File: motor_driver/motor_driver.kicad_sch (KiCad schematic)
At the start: 65 parts, among them J1 Conn_01x01_Socket, J2 Conn_01x01_Socket, J3 Conn_01x01_Socket, J4 Conn_01x03_Pin, J5 Conn_01x06_Pin, Q1 STB19NF20_T-220, Q2 STB19NF20_T-220, Q3 STB19NF20_T-220, Q4 STB19NF20_T-220, Q5 STB19NF20_T-220, Q6 STB19NF20_T-220, U1 INA241A2xD, U3 IR2110, U4 INA241A2xD, U6 IR2110, U7 INA241A2xD, U9 IR2110

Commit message: Change to isolation amp
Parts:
- removed D2: 1N4007, Diode_THT:D_DO-41_SOD81_P10.16mm_Horizontal, symbol Diode:1N4007
- removed J1, J2, J3: Conn_01x01_Socket, symbol Connector:Conn_01x01_Socket
- removed J4: Conn_01x03_Pin, Connector_PinHeader_2.54mm:PinHeader_1x03_P2.54mm_Vertical, symbol Connector:Conn_01x03_Pin
- removed R12, R19: R_Shunt, Custom_footprints:BVT-I-R003, symbol Device:R_Shunt
- removed U1, U4, U7: INA241A2xD, Package_SO:SOIC-8_3.9x4.9mm_P1.27mm, symbol Amplifier_Current:INA241A2xD
- removed U5, U8: ~, Custom_footprints:MCT6, symbol Custom_schematics:MCT6
- removed U6, U9: IR2110, Package_DIP:DIP-14_W7.62mm, symbol Driver_FET:IR2110
- added C22, C35: 10nF, symbol Device:C
- added C23, C26, C27, C29, C31, C33, C36, C39: 100nF, symbol Device:C
- added C24, C28, C32, C34, C37: 22uF, symbol Device:C
- added C25, C30, C38: 330pF, symbol Device:C
- added D2, D4, D6: BZX384xxxx, Diode_SMD:D_SOD-323, symbol Diode:BZX384xxxx
- added D5: 1N4007, Diode_THT:D_DO-41_SOD81_P10.16mm_Horizontal, symbol Diode:1N4007
- added J1: Conn_01x03_Pin, Connector_PinHeader_2.54mm:PinHeader_1x03_P2.54mm_Vertical, symbol Connector:Conn_01x03_Pin
- added J2: Conn_01x05_Pin, Connector_PinHeader_1.00mm:PinHeader_1x05_P1.00mm_Vertical, symbol Connector:Conn_01x05_Pin
- added R12, R19, R22, R27, R33, R35, R38, R43: 3.3k, symbol Device:R
- added R23, R24, R39, R40: 1k, symbol Device:R
- added R25, R41: 30, symbol Device:R
- added R26, R29, R42, R45: 100, symbol Device:R
- added R28, R44: R_Shunt, Custom_footprints:BVT-I-R003, symbol Device:R_Shunt
- added R30, R34, R37, R46: 10, symbol Device:R
- added R31, R32, R47, R48: 10k, symbol Device:R
- added R36: 2k, symbol Device:R
- added U1, U12, U7: AMC1302DWVR, Package_SO:SOIC-8_7.5x5.85mm_P1.27mm, symbol Custom_schematics:AMC1302DWVR
- added U10, U15: IR2110, Package_DIP:DIP-14_W7.62mm, symbol Driver_FET:IR2110
- added U11, U13, U16, U4, U5, U8: TLV6001DCK, Package_TO_SOT_SMD:SOT-353_SC-70-5, symbol Amplifier_Operational:TLV6001DCK
- added U14, U9: ~, Custom_footprints:MCT6, symbol Custom_schematics:MCT6
- added U6: uA7805, symbol Regulator_Linear:uA7805
- C11: value 22uF -> 330pF
- C12, C17: value 100nF -> 330pF
- C14, C16, C18: value 22uF -> 100nF
- C15, C19: value 100nF -> 22uF
- C5: value 100nF -> 10nF
- Q1, Q2, Q3, Q4, Q5, Q6: value STB19NF20_T-220 -> STB19NF20
- R10: value 30 -> 2k
- R11, R13: value 100 -> 3.3k
- R14: value 10 -> 3.3k
- R15, R16: value 1k -> 10k
- R17: value 30 -> 3.3k
- R18: value 100 -> 10
- R20: value 100 -> 2k
- R8, R9: value 1k -> 10
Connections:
- net +15V: now also C20.1, C21.1, C33.1, C34.1, D5.2 (A), U10.3 (VCC), U15.3 (VCC), U6.1 (IN); no longer C10.1, C11.1, C17.1, C18.1
- net +5V: now also C18.1, C19.1, C31.1, C32.1, R23.1, R24.1, R39.1, R40.1, U10.9 (VDD), U15.9 (VDD), U6.3 (OUT); no longer C15.1, C16.1, C8.1, C9.1, R15.1, R16.1, R8.1, R9.1
- net GND: now also C20.2, C21.2, C31.2, C32.2, C33.2, C34.2, U10.11 (SD), U10.13 (VSS), U10.2 (COM), U14.5 (EM), U14.8 (EM), U15.11 (SD), U15.13 (VSS), U15.2 (COM), U6.2 (GND), U9.5 (EM), U9.8 (EM); no longer C10.2, C11.2, C12.2, C15.2, C16.2, C17.2, C5.2, C8.2, C9.2, U2.2 (CA), U2.3 (CA)
- net HI_B: now also R26.1; no longer R11.1
- net HI_C: now also R42.1; no longer R18.1
- net I_A: now also C12.1, R13.2, J2.1 (Pin_1), U4.4
- net I_B: now also C17.1, R17.2, J2.2 (Pin_2), U8.4
- net I_C: now also C30.1, J2.3 (Pin_3), R33.2, U13.4
- net LO_B: now also R29.1; no longer R13.1
- net LO_C: now also R45.1; no longer R20.1
- net PHASE_A: now also J1.1 (Pin_1)
- net PHASE_B: now also J1.2 (Pin_2), R28.4
- net PHASE_C: now also J1.3 (Pin_3), R44.4
- net at R18.2: now also U7.2 (INP)
- net at R20.2: now also D3.1 (K), C23.1, C24.1, U10.6 (VB)
- net MCU_GND: now reaches R16.2
- net MCU_GND: now also C10.2, C13.2, C14.2, C15.2, C16.2, C8.2, C9.2, U2.2 (CA), U2.3 (CA), C26.2, C27.2, C28.2, C29.2, C39.2, J2.5 (Pin_5), R32.2, R48.2, U1.5 (GND2), U11.2 (V-), U12.5 (GND2), U13.2 (V-), U14.2 (CA), U14.3 (CA), U16.2 (V-), U4.2 (V-), U5.2 (V-), U7.5 (GND2), U8.2 (V-), U9.2 (CA), U9.3 (CA)
- net at R15.2: now also R16.1, U5.1 (+)
- net +3.3V: now reaches C13.1, C14.1
- net +3.3V: now also C10.1, C15.1, C16.1, C8.1, C9.1, R15.1, C26.1, C27.1, C28.1, C29.1, C39.1, J2.4 (Pin_4), R31.1, R47.1, U1.8 (VDD2), U11.5 (V+), U12.8 (VDD2), U13.5 (V+), U16.5 (V+), U4.5 (V+), U5.5 (V+), U7.8 (VDD2), U8.5 (V+)
- net at Q3.3 (S), Q4.2 (D): now also C23.2, C24.2, D4.2 (A), R28.1, U10.5 (VS), U7.4 (GND1); no longer C13.2, C14.2
- net at R21.2: now also U7.3 (INN); no longer Q6.1 (G)
- net at Q5.3 (S), Q6.2 (D): now also C36.2, C37.2, D6.2 (A), R44.1, U12.4 (GND1), U15.5 (VS); no longer C20.2, C21.2
- net at C6.1, C7.1, D1.1 (K)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: now also R10.2
- net at C6.2, C7.2, Q1.3 (S)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: now also D2.2 (A), U1.4 (GND1)
- net at R14.2: now also C11.2, U5.3 (-), U5.4; no longer Q4.1 (G)
- net at R8.2: now also U1.2 (INP)
- net at R21.1: now also C22.2, R28.2
- net at R14.1: now also C11.1, R11.2, U4.3 (-)
- net at R9.2: now also U1.3 (INN)
- net at R10.1: now also D2.1 (K), U1.1 (VDD1)
- net at R17.1: now also C17.2, R19.2, U8.1 (+)
- net at Q5.1 (G): now also R41.2; no longer R17.2
- net at R5.2: now also C5.2, R9.1
- net at R5.3: now also C5.1, R8.1
- net at Q3.1 (G): now also R25.2; no longer R10.2
- removed net +3V3: C12.1, C19.1, C5.1
- new net: R42.2, U14.1 (AN)
- new net: D4.1 (K), R20.1, U7.1 (VDD1)
- new net: R22.1, U7.6 (OUTN)
- new net: R19.1, U7.7 (OUTP)
- new net: C30.2, R33.1, R35.2, U13.1 (+)
- new net: R46.1, U15.1 (LO)
- new net: R39.2, U14.7 (COL), U15.10 (HIN)
- new net: R40.2, U14.6 (COL), U15.12 (LIN)
- new net: C36.1, C37.1, D5.1 (K), R36.2, U15.6 (VB)
- new net: R41.1, U15.7 (HO)
- new net: R12.1, U1.7 (OUTP)
- new net: C12.2, R12.2, R13.1, U4.1 (+)
- new net: R31.2, R32.1, U11.1 (+)
- new net: R23.2, U10.10 (HIN), U9.7 (COL)
- new net: C38.1, R38.2, R43.1, U13.3 (-)
- new net: C25.1, R22.2, R27.1, U8.3 (-)
- new net: C25.2, R27.2, U11.3 (-), U11.4
- new net: R47.2, R48.1, U16.1 (+)
- new net: C38.2, R43.2, U16.3 (-), U16.4
- new net: R11.1, U1.6 (OUTN)
- new net: R35.1, U12.7 (OUTP)
- new net: R29.2, U9.4 (AN)
- new net: C35.1, R34.1, R44.3
- new net: C35.2, R37.1, R44.2
- new net: R38.1, U12.6 (OUTN)
- new net: C22.1, R18.1, R28.3
- new net: Q6.1 (G), R46.2
- new net: R45.2, U14.4 (AN)
- new net: R30.1, U10.1 (LO)
- new net: Q4.1 (G), R30.2
- new net: R24.2, U10.12 (LIN), U9.6 (COL)
- new net: D6.1 (K), R36.1, U12.1 (VDD1)
- new net: R26.2, U9.1 (AN)
- new net: R34.2, U12.2 (INP)
- new net: R25.1, U10.7 (HO)
- new net: R37.2, U12.3 (INN)
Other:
- moved on the sheet: C1, C2, C3, C4, C6, C7, D1, J5, Q1, Q2, R1, R2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

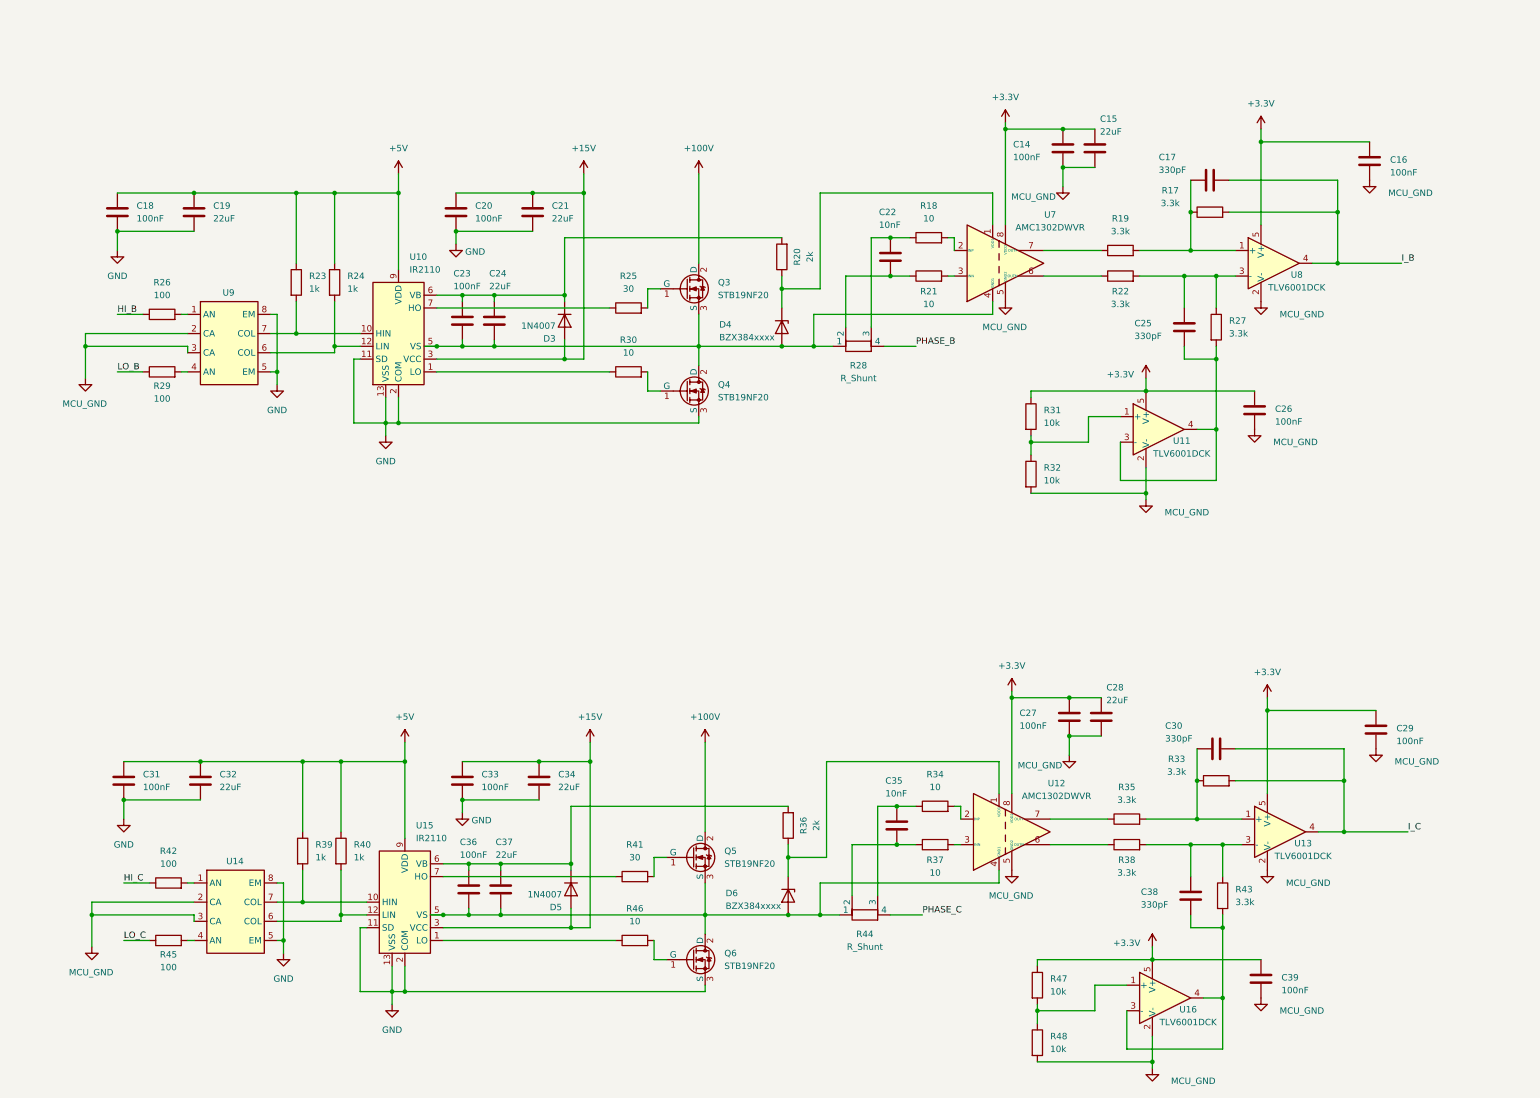
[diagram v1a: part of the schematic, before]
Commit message: Add footprints
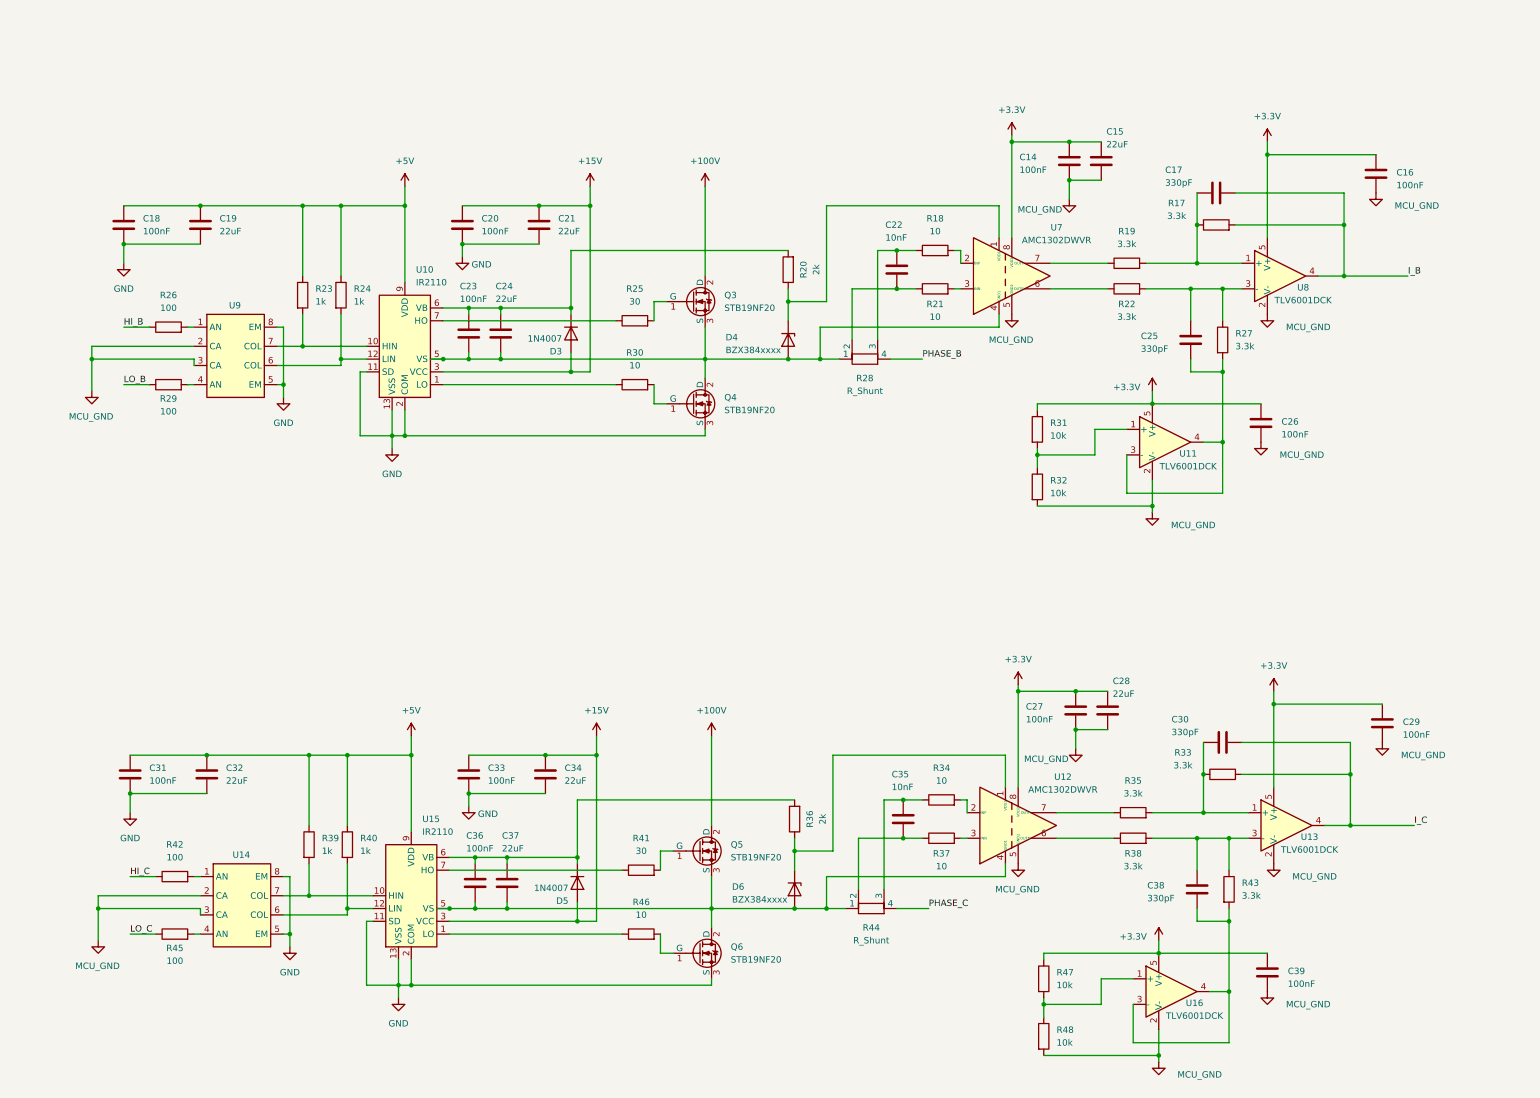
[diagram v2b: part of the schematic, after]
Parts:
- C1, C10, C13, C14, C16, C18, C20, C23, C26, C27, C29, C3, C31, C33, C36, C39, C6, C8: footprint (none) -> Capacitor_SMD:C_0603_1608Metric_Pad1.08x0.95mm_HandSolder
- C11, C12, C17, C22, C25, C30, C35, C38, C5: footprint (none) -> Capacitor_SMD:C_0402_1005Metric_Pad0.74x0.62mm_HandSolder
- C15, C19, C2, C21, C24, C28, C32, C34, C37, C4, C7, C9: footprint (none) -> Capacitor_SMD:C_0805_2012Metric
- R1, R11, R12, R13, R14, R15, R16, R17, R19, R2, R22, R23, R24, R26, R27, R29, R31, R32, R33, R35, R38, R39, R4, R40, R42, R43, R45, R47, R48, R6: footprint (none) -> Resistor_SMD:R_0805_2012Metric_Pad1.20x1.40mm_HandSolder
- R10, R20, R36: footprint (none) -> Resistor_SMD:R_1206_3216Metric
- R18, R21, R25, R3, R30, R34, R37, R41, R46, R7, R8, R9: footprint (none) -> Resistor_SMD:R_1206_3216Metric_Pad1.30x1.75mm_HandSolder
- U6: footprint (none) -> Package_TO_SOT_THT:TO-220-3_Vertical

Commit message: Minor component changes
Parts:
- removed C14, C16: 100nF, Capacitor_SMD:C_0603_1608Metric_Pad1.08x0.95mm_HandSolder, symbol Device:C
- removed C15, C9: 22uF, Capacitor_SMD:C_0805_2012Metric, symbol Device:C
- added C11, C40, C42, C45, C47, C50: 100nF, Capacitor_SMD:C_0603_1608Metric_Pad1.08x0.95mm_HandSolder, symbol Device:C
- added C12, C2, C46: 1uF, Capacitor_SMD:C_0805_2012Metric_Pad1.18x1.45mm_HandSolder, symbol Device:C
- added C4, C41, C43, C48, C51: 22uF, Capacitor_SMD:C_0805_2012Metric_Pad1.18x1.45mm_HandSolder, symbol Device:C
- added C44: 10nF, Capacitor_SMD:C_0402_1005Metric_Pad0.74x0.62mm_HandSolder, symbol Device:C
- added C49: 330pF, Capacitor_SMD:C_0402_1005Metric_Pad0.74x0.62mm_HandSolder, symbol Device:C
- added J1, J2: Conn_01x02_Pin, TerminalBlock:TerminalBlock_MaiXu_MX126-5.0-02P_1x02_P5.00mm, symbol Connector:Conn_01x02_Pin
- C14: renamed from C7; footprint Capacitor_SMD:C_0805_2012Metric -> Capacitor_SMD:C_0805_2012Metric_Pad1.18x1.45mm_HandSolder
- C17, C38: value 330pF -> 22uF; footprint Capacitor_SMD:C_0402_1005Metric_Pad0.74x0.62mm_HandSolder -> Capacitor_SMD:C_0805_2012Metric_Pad1.18x1.45mm_HandSolder
- C19: value 22uF -> 1uF; footprint Capacitor_SMD:C_0805_2012Metric -> Capacitor_SMD:C_0805_2012Metric_Pad1.18x1.45mm_HandSolder
- C21, C24, C34: footprint Capacitor_SMD:C_0805_2012Metric -> Capacitor_SMD:C_0805_2012Metric_Pad1.18x1.45mm_HandSolder
- C22: value 10nF -> 330pF
- C25, C30: value 330pF -> 100nF; footprint Capacitor_SMD:C_0402_1005Metric_Pad0.74x0.62mm_HandSolder -> Capacitor_SMD:C_0603_1608Metric_Pad1.08x0.95mm_HandSolder
- C26, C31: value 100nF -> 22uF; footprint Capacitor_SMD:C_0603_1608Metric_Pad1.08x0.95mm_HandSolder -> Capacitor_SMD:C_0805_2012Metric_Pad1.18x1.45mm_HandSolder
- C27: value 100nF -> 10nF; footprint Capacitor_SMD:C_0603_1608Metric_Pad1.08x0.95mm_HandSolder -> Capacitor_SMD:C_0402_1005Metric_Pad0.74x0.62mm_HandSolder
- C28, C37: value 22uF -> 100nF; footprint Capacitor_SMD:C_0805_2012Metric -> Capacitor_SMD:C_0603_1608Metric_Pad1.08x0.95mm_HandSolder
- C29, C36: value 100nF -> 1uF; footprint Capacitor_SMD:C_0603_1608Metric_Pad1.08x0.95mm_HandSolder -> Capacitor_SMD:C_0805_2012Metric_Pad1.18x1.45mm_HandSolder
- C32: value 22uF -> 330pF; footprint Capacitor_SMD:C_0805_2012Metric -> Capacitor_SMD:C_0402_1005Metric_Pad0.74x0.62mm_HandSolder
- C35: value 10nF -> 100nF; footprint Capacitor_SMD:C_0402_1005Metric_Pad0.74x0.62mm_HandSolder -> Capacitor_SMD:C_0603_1608Metric_Pad1.08x0.95mm_HandSolder
- C39: value 100nF -> 330pF; footprint Capacitor_SMD:C_0603_1608Metric_Pad1.08x0.95mm_HandSolder -> Capacitor_SMD:C_0402_1005Metric_Pad0.74x0.62mm_HandSolder
- C7: renamed from C2; footprint Capacitor_SMD:C_0805_2012Metric -> Capacitor_SMD:C_0805_2012Metric_Pad1.18x1.45mm_HandSolder
- C9: renamed from C4; footprint Capacitor_SMD:C_0805_2012Metric -> Capacitor_SMD:C_0805_2012Metric_Pad1.18x1.45mm_HandSolder
- D1, D3, D5: value 1N4007 -> UF4007
- J5: renamed from J2; footprint Connector_PinHeader_1.00mm:PinHeader_1x05_P1.00mm_Vertical -> Connector_PinHeader_2.54mm:PinHeader_1x05_P2.54mm_Vertical
- R20, R36: value 2k -> 910; footprint Resistor_SMD:R_1206_3216Metric -> Resistor_SMD:R_1206_3216Metric_Pad1.30x1.75mm_HandSolder
- R4: renamed from R10; value 2k -> 910; footprint Resistor_SMD:R_1206_3216Metric -> Resistor_SMD:R_1206_3216Metric_Pad1.30x1.75mm_HandSolder
- U11, U13, U16, U8: value TLV6001DCK -> TLV6001IDBVR; footprint Package_TO_SOT_SMD:SOT-353_SC-70-5 -> Package_TO_SOT_SMD:SOT-23-5_HandSoldering
- U3: renamed from U4; value TLV6001DCK -> TLV6001IDBVR; footprint Package_TO_SOT_SMD:SOT-353_SC-70-5 -> Package_TO_SOT_SMD:SOT-23-5_HandSoldering
- U6: renamed from U5; value TLV6001DCK -> TLV6001IDBVR; footprint Package_TO_SOT_SMD:SOT-353_SC-70-5 -> Package_TO_SOT_SMD:SOT-23-5_HandSoldering
- renumbered C8 to C1, C5 to C10, C6 to C13, C11 to C15, C13 to C16, C10 to C3, C12 to C5, C1 to C6, C3 to C8, J1 to J3, J5 to J4, R13 to R1, R4 to R10, R14 to R11, R5 to R12, R6 to R13, R7 to R14, R8 to R2, R12 to R3, R9 to R5, R11 to R6, R1 to R7, R2 to R8, R3 to R9, U6 to U1, U1 to U2, U2 to U4, U3 to U5
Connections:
- net +100V: now also J1.1 (Pin_1)
- net +15V: now also C25.1, C26.1, C42.1, C43.1, J2.1 (Pin_1); no longer C20.1, C21.1, C33.1, C34.1
- net +3.3V: now also C17.1, C18.1, C19.1, C20.1, C21.1, C33.1, C34.1, C35.1, C36.1, C37.1, C38.1, C2.1, C4.1, C50.1, C51.1; no longer C26.1, C27.1, C28.1, C29.1, C39.1
- net +5V: now also C23.1, C24.1, C40.1, C41.1; no longer C18.1, C19.1, C31.1, C32.1
- net GND: now also C23.2, C24.2, C25.2, C26.2, C40.2, C41.2, C42.2, C43.2, J1.2 (Pin_2), J2.2 (Pin_2); no longer C18.2, C19.2, C20.2, C21.2, C31.2, C32.2, C33.2, C34.2
- net I_B: now also C22.1; no longer C17.1
- net I_C: now also C39.1; no longer C30.1
- net MCU_GND: now also C17.2, C18.2, C19.2, C20.2, C21.2, C33.2, C34.2, C35.2, C36.2, C37.2, C38.2, C2.2, C4.2, C50.2, C51.2; no longer C26.2, C27.2, C28.2, C29.2, C39.2
- net at R21.1, R28.2: now also C27.2; no longer C22.2
- net at D3.1 (K), R20.2, U10.6 (VB): now also C30.1, C31.1; no longer C23.1, C24.1
- net at D5.1 (K), R36.2, U15.6 (VB): now also C47.1, C48.1; no longer C36.1, C37.1
- net at D6.2 (A), Q5.3 (S), Q6.2 (D)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: now also C45.2, C46.2, C47.2, C48.2; no longer C36.2, C37.2
- net at D4.2 (A), Q3.3 (S), Q4.2 (D)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: now also C28.2, C29.2, C30.2, C31.2; no longer C23.2, C24.2
- net at R18.1, R28.3: now also C27.1; no longer C22.1
- net at C13.2, C14.2, D2.2 (A)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: now also C11.2, C12.2
- net at R34.1, R44.3: now also C44.1; no longer C35.1
- net at R33.1, R35.2, U13.1 (+): now also C39.2; no longer C30.2
- net at D4.1 (K), R20.1, U7.1 (VDD1): now also C28.1, C29.1
- net at R17.1, R19.2, U8.1 (+): now also C22.2; no longer C17.2
- net at R22.2, R27.1, U8.3 (-): now also C32.1; no longer C25.1
- net at R37.1, R44.2: now also C44.2; no longer C35.2
- net at R27.2, U11.3 (-), U11.4: now also C32.2; no longer C25.2
- net at D2.1 (K), R4.1, U2.1 (VDD1): now also C11.1, C12.1
- net at R38.2, R43.1, U13.3 (-): now also C49.1; no longer C38.1
- net at R43.2, U16.3 (-), U16.4: now also C49.2; no longer C38.2
- net at D6.1 (K), R36.1, U12.1 (VDD1): now also C45.1, C46.1
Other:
- moved on the sheet: C1, C10, C13, C14, C15, C16, C3, C5, C6, C7, C8, C9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
